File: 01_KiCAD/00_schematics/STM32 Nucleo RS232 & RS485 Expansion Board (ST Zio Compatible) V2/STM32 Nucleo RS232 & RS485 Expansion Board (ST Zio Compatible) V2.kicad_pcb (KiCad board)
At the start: 4 copper layers, 72 x 133.4 mm, 186 parts, among them CN10 Conn_02x17_Odd_Even, CN7 Conn_02x10_Odd_Even, CN8 Conn_02x08_Odd_Even, CN9 Conn_02x15_Odd_Even, J1 HD-A(Y), J10 SW_ENA, J11 MODE0, J12 MODE1, J13 MODE2, J14 DIR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

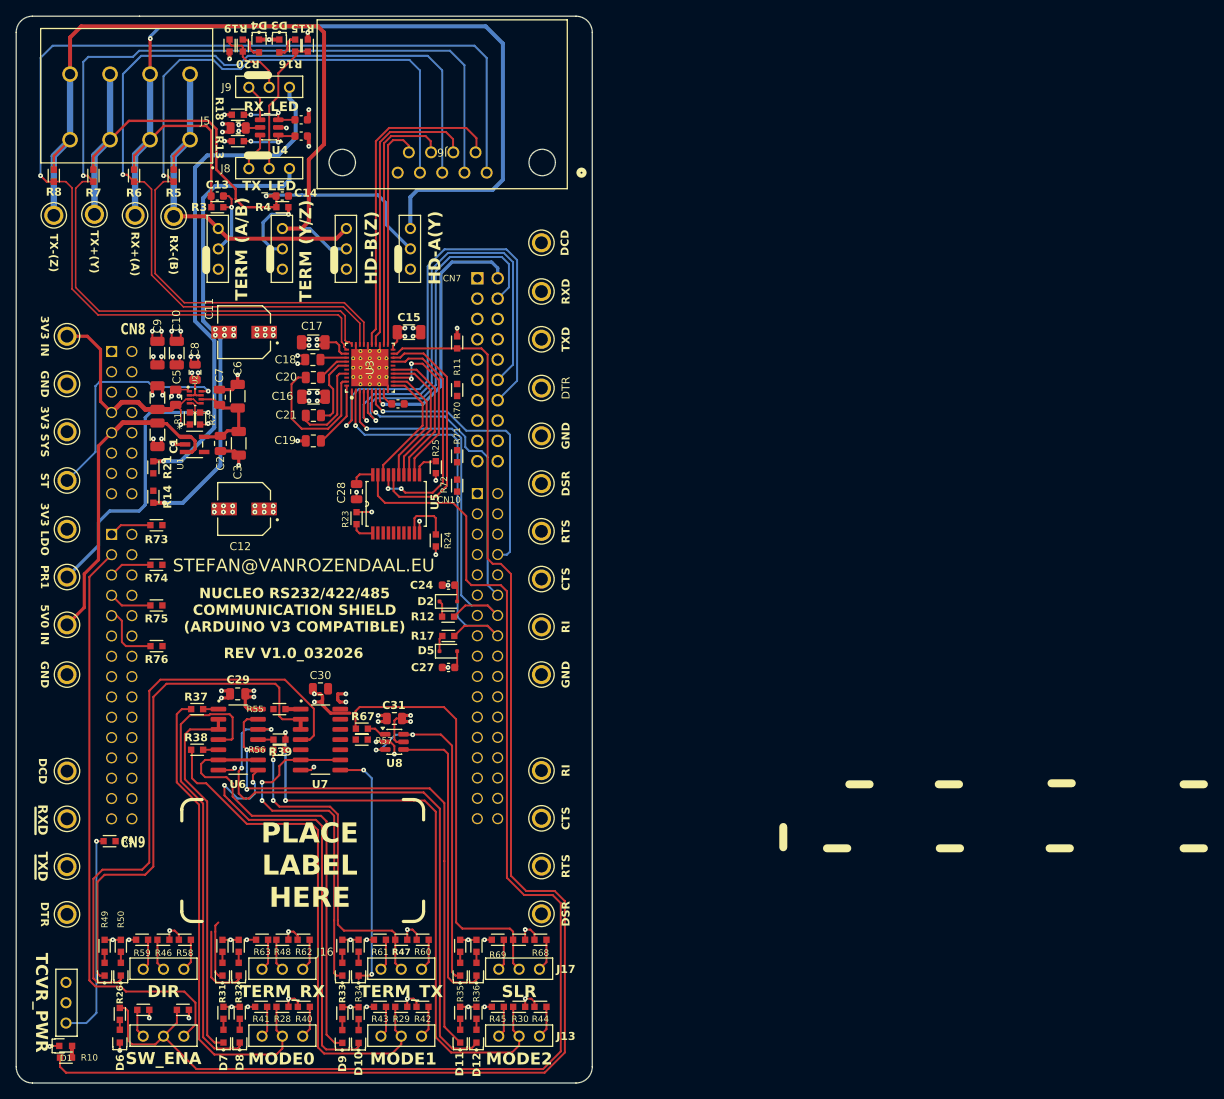
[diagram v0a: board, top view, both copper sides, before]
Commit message: Finalizing board layout & routing
Set HW Revision of board to: HW REV A0.1 and placed this as copper text on the back of the PCB.
Run DRC to see any critical errors. Resolved some minor silkscreen issues with overlapping text.
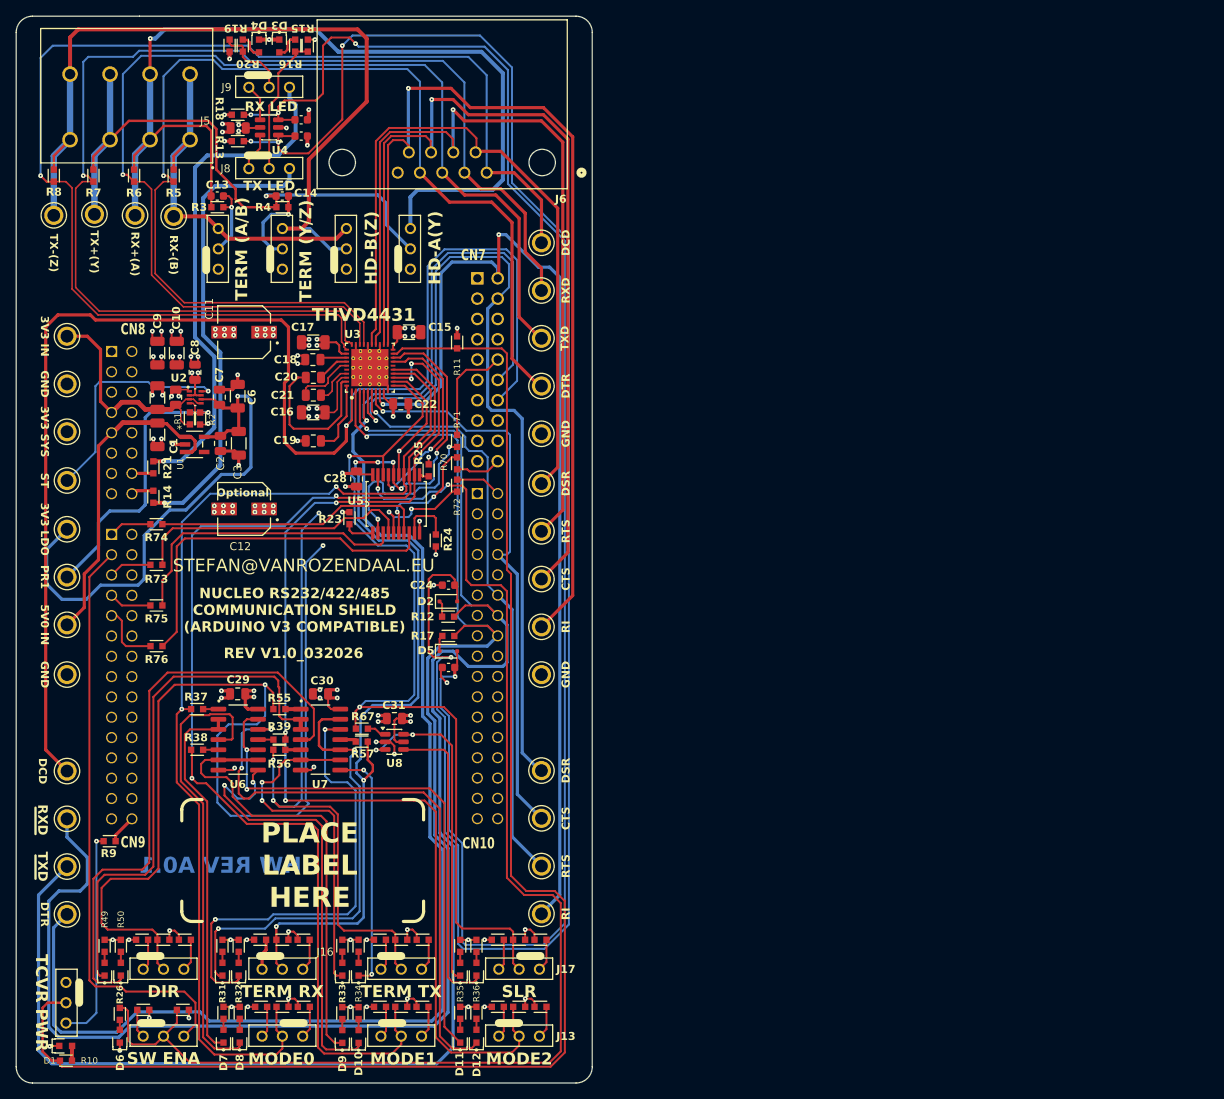
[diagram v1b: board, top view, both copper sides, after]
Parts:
- C22: footprint PCM_SparkFun-Capacitor:C_0603_1608Metric -> Capacitor_SMD:C_0805_2012Metric
- J10: value SW_ENA -> SW ENA
- J15: value TERM_TX -> TERM TX
- J16: value TERM_RX -> TERM RX
- J7: value TCVR_PWR -> TCVR PWR
- J8: value TX_LED -> TX LED
- J9: value RX_LED -> RX LED
- TP21: value DSR -> RI
- TP27: value RI -> DSR
- U3: value THVD4431RHAR -> THVD4431
- moved R70 6.37 mm to (82.9, 89.9)
- moved R74 5.08 mm to (45.3, 100.3)
- moved R73 4.95 mm to (45.3, 105.4)
- moved C21 2.54 mm to (65.0, 84.2), turned to 180 degrees
- moved C16 1.96 mm to (64.9, 86.4)
- moved C28 1.59 mm to (70.4, 94.7)
- moved R25 0.97 mm to (79.4, 93.6), turned to 90 degrees
- moved R23 0.89 mm to (69.5, 99.6)
- moved R71 0.89 mm to (82.9, 92.7)
- moved C30 0.64 mm to (65.8, 121.5), turned to 180 degrees
- moved R10 0.38 mm to (34.0, 167.4)
- moved C22 0.35 mm to (75.9, 85.3)
- moved TP22 0.25 mm to (93.5, 89.0)
- moved R57 0.25 mm to (71.0, 127.5)
- moved TP19 0.25 mm to (93.5, 83.1)
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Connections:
- net /RS232 & RS485 Tranceiver/CTSBus renamed CTSBus
- net /RS232 & RS485 Tranceiver/DSRBus renamed DSRBus
- net /RS232 & RS485 Tranceiver/RIBus renamed RIBus
- net /RS232 & RS485 Tranceiver/RTSBus renamed RTSBus
- net /RS232 & RS485 Tranceiver/RX+ renamed RX+
- net /RS232 & RS485 Tranceiver/RX- renamed RX-
- net /RS232 & RS485 Tranceiver/TX+ renamed TX+
- net /RS232 & RS485 Tranceiver/TX- renamed TX-
- R73 pad 1: Net-(CN9-Pin_1) -> Net-(CN9-Pin_5)
- R74 pad 1: Net-(CN9-Pin_5) -> Net-(CN9-Pin_1)
- TP21 pad TP: L5-DSR -> L8-RI
- TP27 pad TP: L8-RI -> L5-DSR
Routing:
- net /Rx & Tx LED/TX_RC: track 9.32 -> 233.1 mm, vias 2 -> 4
- net /Rx & Tx LED/RX_RC: track 9.31 -> 208.3 mm, vias 2 -> 4
- net L4-DTR: track 56.9 -> 203.7 mm
- net L3-TXD: track 49.2 -> 193.5 mm
- net DIR: track 19.9 -> 163.5 mm, vias 0 -> 3
- net L2-RXD: track 52.4 -> 190.2 mm
- net L1-DCD: track 64.4 -> 178.0 mm
- net L8-RI: track 33.4 -> 129.3 mm, vias 1 -> 2
- net RIBus: track 28.9 -> 122.8 mm, vias 0 -> 1
- net TERM_RX: track 35.3 -> 126.2 mm, vias 0 -> 7
- net CTSBus: track 33.0 -> 115.1 mm, vias 0 -> 1
- net RTSBus: track 37.2 -> 107.7 mm, vias 0 -> 1
- net L5-DSR: track 45.0 -> 109.0 mm
- net MODE1: track 83.8 -> 146.1 mm, vias 0 -> 2
- net 3V3_LDO: track 12.7 -> 68.7 mm, vias 0 -> 1
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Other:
- board text added: "HW REV A0.1"

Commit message: Final revision checkup
After BOM-update and corrected some footprints and package sizes for resistors and capacitors, updated the PCB to "HW REV A0.2" as final PCB layout. Need to run DRC check before final approval.
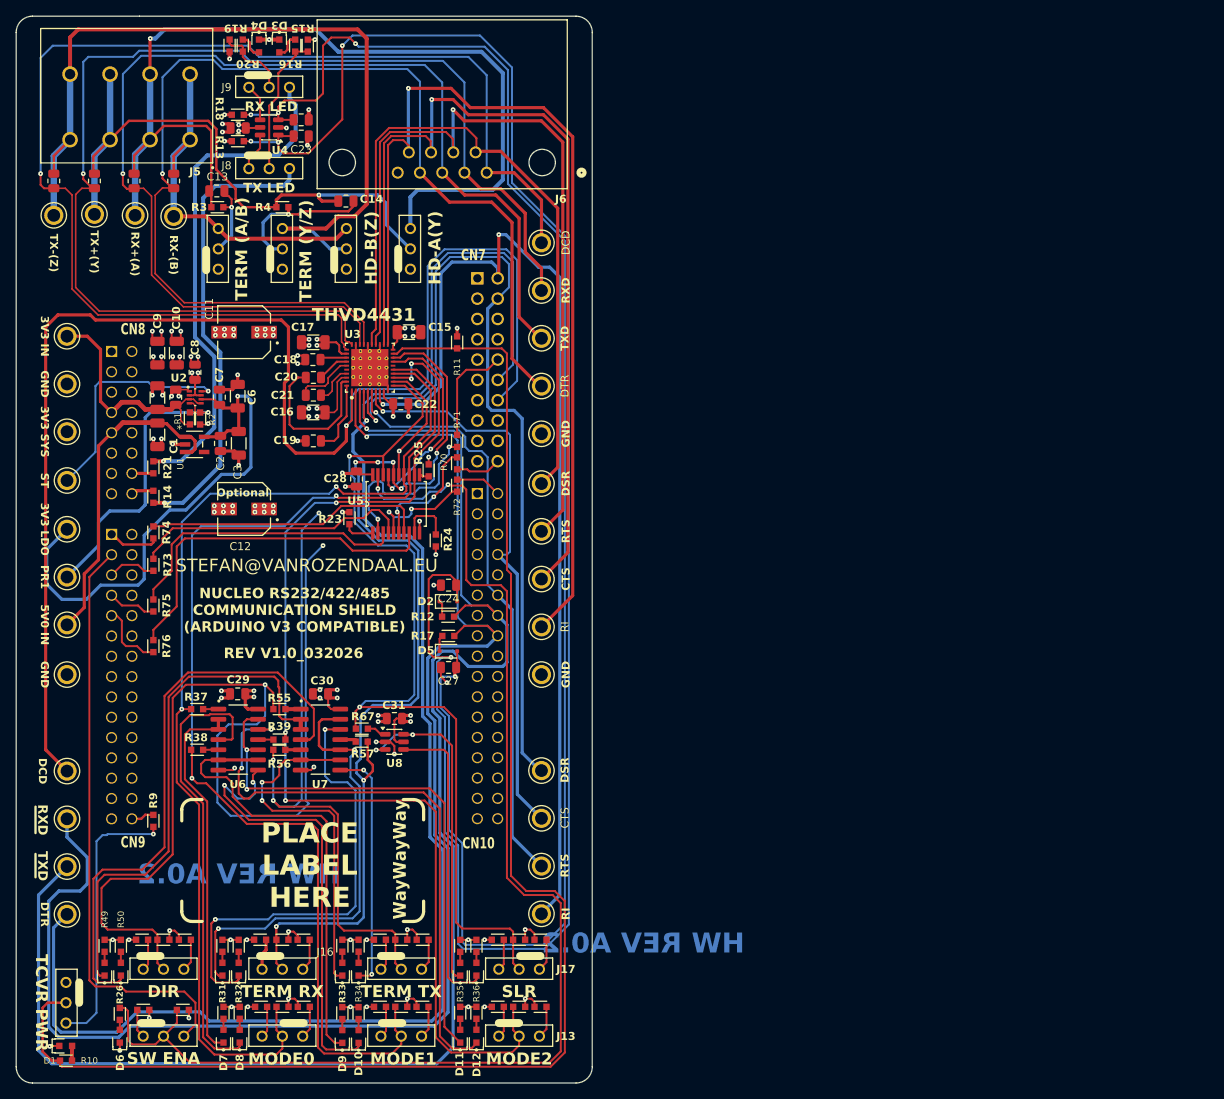
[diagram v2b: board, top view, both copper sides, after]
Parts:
- C13, C14, C23, C24, C26, C27: footprint PCM_SparkFun-Capacitor:C_0603_1608Metric -> Capacitor_SMD:C_0805_2012Metric
- C4, C6, C9: value 1µ -> 1µF
- CN10: value Conn_02x17_Odd_Even -> SSW-117-23-G-D
- CN7: value Conn_02x10_Odd_Even -> SSW-110-23-G-D
- CN8: value Conn_02x08_Odd_Even -> SSW-108-23-G-D
- CN9: value Conn_02x15_Odd_Even -> SSW-115-23-G-D
- J5: value 1190299 -> TERM BLK 4POS 5mm TH
- R5, R6, R7, R8: footprint PCM_fab:R_0603 -> PCM_SparkFun-Resistor:R_0805_2012Metric
- TP10, TP19, TP30: footprint 5122_Blue:KEYSTONE_5122 -> 5121_Green:KEYSTONE_5121
- TP12, TP15, TP23, TP25, TP27: footprint 5121_Green:KEYSTONE_5121 -> 5122_Blue:KEYSTONE_5122
- moved C14 7.98 mm to (69.0, 59.9)
- moved R9 6.03 mm to (45.0, 137.4), turned to 90 degrees
- moved R74 1.10 mm to (45.0, 101.4), turned to 90 degrees
- moved R7 0.68 mm to (37.6, 57.4)
- moved R5 0.67 mm to (47.5, 57.4)
- moved R6 0.67 mm to (42.5, 57.4)
- moved R8 0.67 mm to (32.5, 57.4)
- moved C13 0.64 mm to (52.9, 58.7)
- moved R76 0.39 mm to (45.0, 115.6), turned to -90 degrees
- moved R73 0.38 mm to (45.0, 105.4), turned to 90 degrees
- moved R75 0.38 mm to (45.0, 110.5), turned to 90 degrees
- turned TP19 to 90 degrees
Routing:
- net Net-(J7-Pin_3): track 26.7 -> 34.2 mm
- net Net-(J4-Pin_2): track 11.0 -> 18.2 mm
- net TX- (Z): track 104.2 -> 107.2 mm
- net MCU_MODE1: track 34.2 -> 35.9 mm
- net Net-(D14-K): track 74.6 -> 73.1 mm
- net Net-(D13-K): track 66.9 -> 65.8 mm
- net Net-(CN9-Pin_1): track 5.38 -> 6.36 mm
- net Net-(CN9-Pin_5): track 5.38 -> 6.32 mm
- net DIR: track 163.5 -> 162.7 mm
- net Net-(CN9-Pin_9): track 8.12 -> 8.93 mm
- net MCU_SHDN: track 3.64 -> 2.89 mm
- net Net-(CN9-Pin_7): track 5.50 -> 6.07 mm
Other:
- board text added: "HW REV A0.2"
- board text added: "WayWayWay"
- board text removed: "HW REV A0.1"

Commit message: Updated PCB Layout
Moved the 4x RS485 testpoints closer to the Phoenix connector so the longer testpoints don't interfere with the added LCD shield when stacked together.
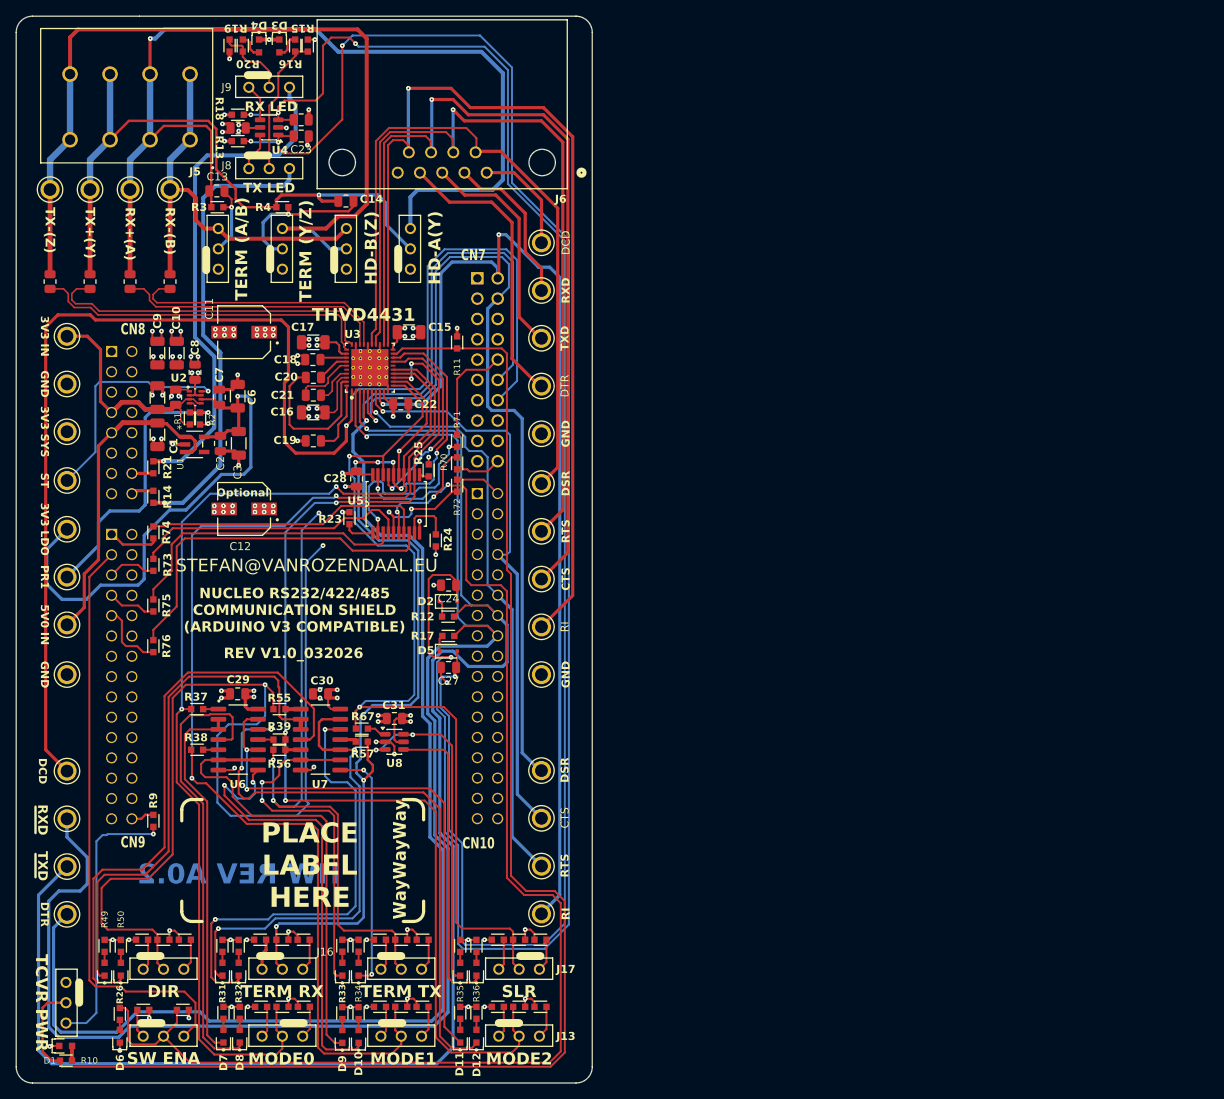
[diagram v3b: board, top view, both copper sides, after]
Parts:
- moved R7 12.6 mm to (37.0, 70.0)
- moved R6 12.6 mm to (42.0, 70.0)
- moved R8 12.6 mm to (32.0, 70.0)
- moved R5 12.6 mm to (47.0, 70.0)
- moved TP20 3.38 mm to (47.0, 58.5)
- moved TP17 3.28 mm to (42.0, 58.5)
- moved TP11 3.26 mm to (32.0, 58.5)
- moved TP14 3.14 mm to (37.0, 58.5), turned to 0 degrees
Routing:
- net TX-: track 155.3 -> 56.3 mm, vias 1 -> 0
- net TX+: track 151.2 -> 62.7 mm, vias 1 -> 0
- net RX+: track 140.9 -> 61.9 mm, vias 1 -> 0
- net RX-: track 140.3 -> 69.9 mm, vias 1 -> 0
- net RX- (B): track 46.5 -> 52.3 mm
- net RX+ (A): track 122.0 -> 125.2 mm
- net TX- (Z): track 107.2 -> 110.2 mm
- net TX+ (Y): track 78.2 -> 81.1 mm

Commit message: Updated PCB
Re-aligned all testpoints. Set fixed distance of 6mm from each testpoint to neighbour one. Set board outline to match exactly the dimensions of 133x72mm
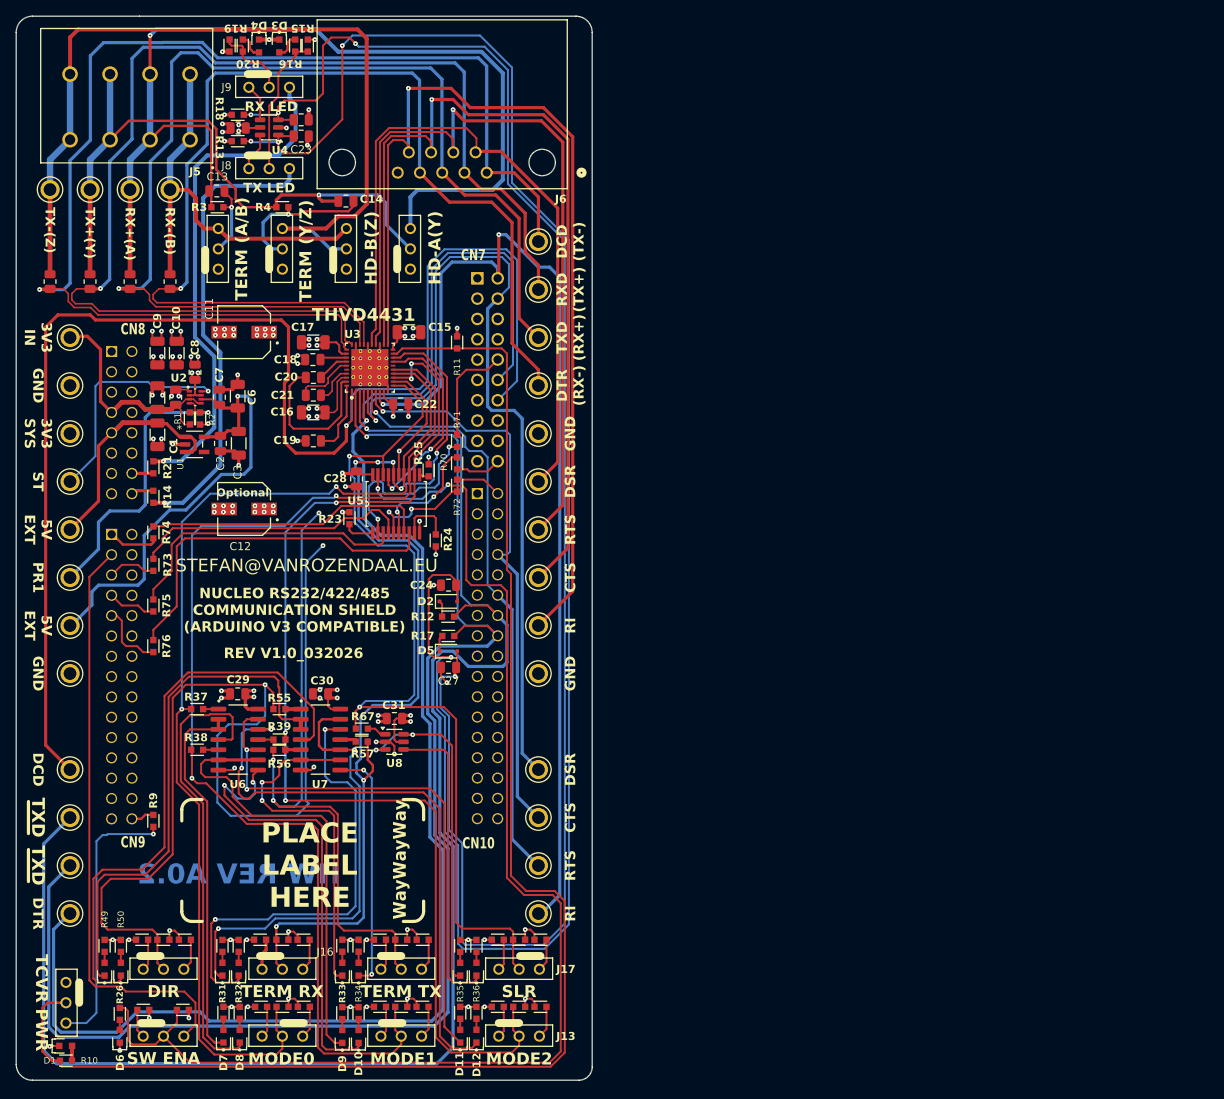
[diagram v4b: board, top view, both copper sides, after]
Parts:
- moved TP3 12.0 mm to (34.5, 113.0)
- moved TP2 11.9 mm to (34.5, 101.0)
- moved TP15 6.14 mm to (34.5, 137.0)
- moved TP12 5.85 mm to (34.5, 143.0)
- moved TP24 0.46 mm to (93.1, 95.0)
- moved TP6 0.44 mm to (34.5, 89.0)
- moved TP26 0.44 mm to (93.1, 101.0)
- moved TP4 0.43 mm to (34.5, 83.0), turned to 0 degrees
- moved TP9 0.43 mm to (34.5, 131.0)
- moved TP28 0.42 mm to (93.1, 107.0)
- moved TP5 0.42 mm to (34.5, 77.0)
- moved TP30 0.41 mm to (93.1, 113.0)
- moved TP10 0.41 mm to (93.1, 65.0)
- moved TP8 0.40 mm to (34.5, 95.0)
- moved TP27 0.40 mm to (93.1, 131.0)
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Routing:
- net TX-: track 56.3 -> 155.8 mm, vias 0 -> 1
- net TX+: track 62.7 -> 150.0 mm, vias 0 -> 1
- net RX+: track 61.9 -> 142.9 mm, vias 0 -> 1
- net RX-: track 69.9 -> 137.0 mm, vias 0 -> 1
- net ARDUINO_5V: track 40.6 -> 28.6 mm
- net L2-RXD: track 190.2 -> 180.9 mm
- net 3V3_LDO: track 68.7 -> 59.4 mm
- net L3-TXD: track 193.5 -> 198.9 mm
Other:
- board size 72 x 133.4 mm -> 72 x 133 mm
- board text added: "3V3 IN"
- board text added: "3V3 SYS"
- board text added: "5V EXT"
- board text added: "CTS"
- board text added: "DCD"
- board text added: "DCD (TX-)"
- board text added: "DSR"
- board text added: "DTR"
- board text added: "DTR (RX-)"
- board text added: "GND"
- board text added: "PR1"
- board text added: "RI"
- board text added: "RTS"
- board text added: "RXD (TX+)"
- board text added: "ST"
- board text added: "TXD"
- board text added: "TXD (RX+)"
